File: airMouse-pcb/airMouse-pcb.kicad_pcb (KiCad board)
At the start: 2 copper layers, 54 parts, among them Q1 IRLML6346, SW1 TACT, SW10 TACT, SW11 TACT, SW12 TACT, SW13 TACT, SW14 TACT, SW15 TACT, SW16 TACT, SW17 TACT, SW18 TACT, SW19 TACT, SW2 TACT, SW20 TACT, SW21 TACT, SW22 TACT, SW23 TACT, SW24 TACT, SW25 TACT, SW26 TACT, SW27 TACT, SW28 TACT, SW29 TACT, SW3 TACT, SW30 TACT, SW31 TACT, SW32 TACT, SW33 TACT, SW34 TACT, SW35 TACT, SW36 TACT, SW37 TACT, SW38 TACT, SW39 TACT, SW4 TACT, SW40 TACT, SW41 TACT, SW42 TACT, SW43 TACT, SW44 TACT, SW45 TACT, SW46 TACT, SW47 TACT, SW48 TACT, SW49 TACT, SW5 TACT, SW6 TACT, SW7 TACT, SW8 TACT, SW9 TACT, U1 STM32G071RBTx, U2 AP1603

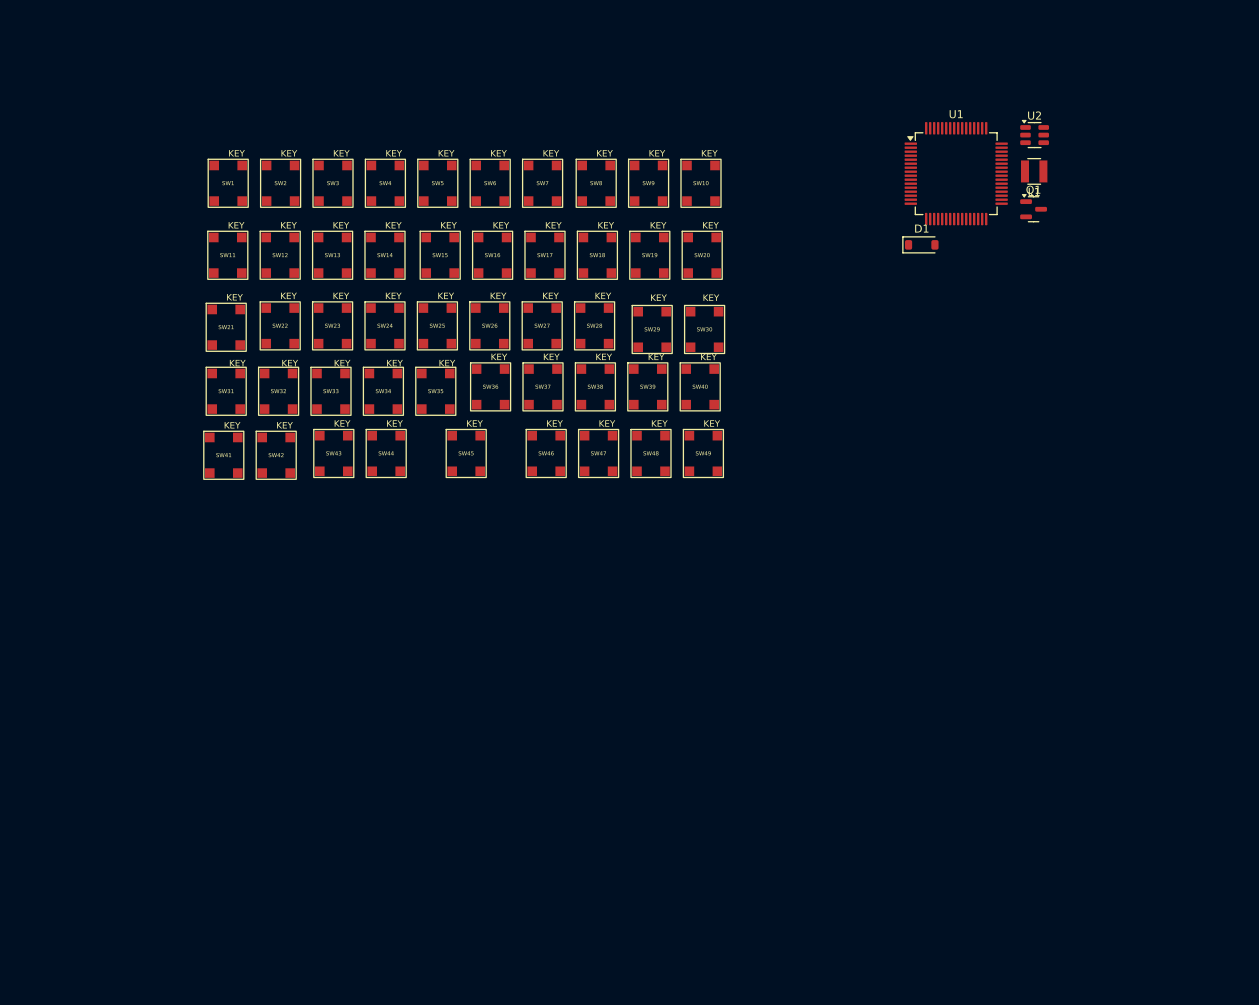
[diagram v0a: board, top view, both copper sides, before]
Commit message: add keyboard
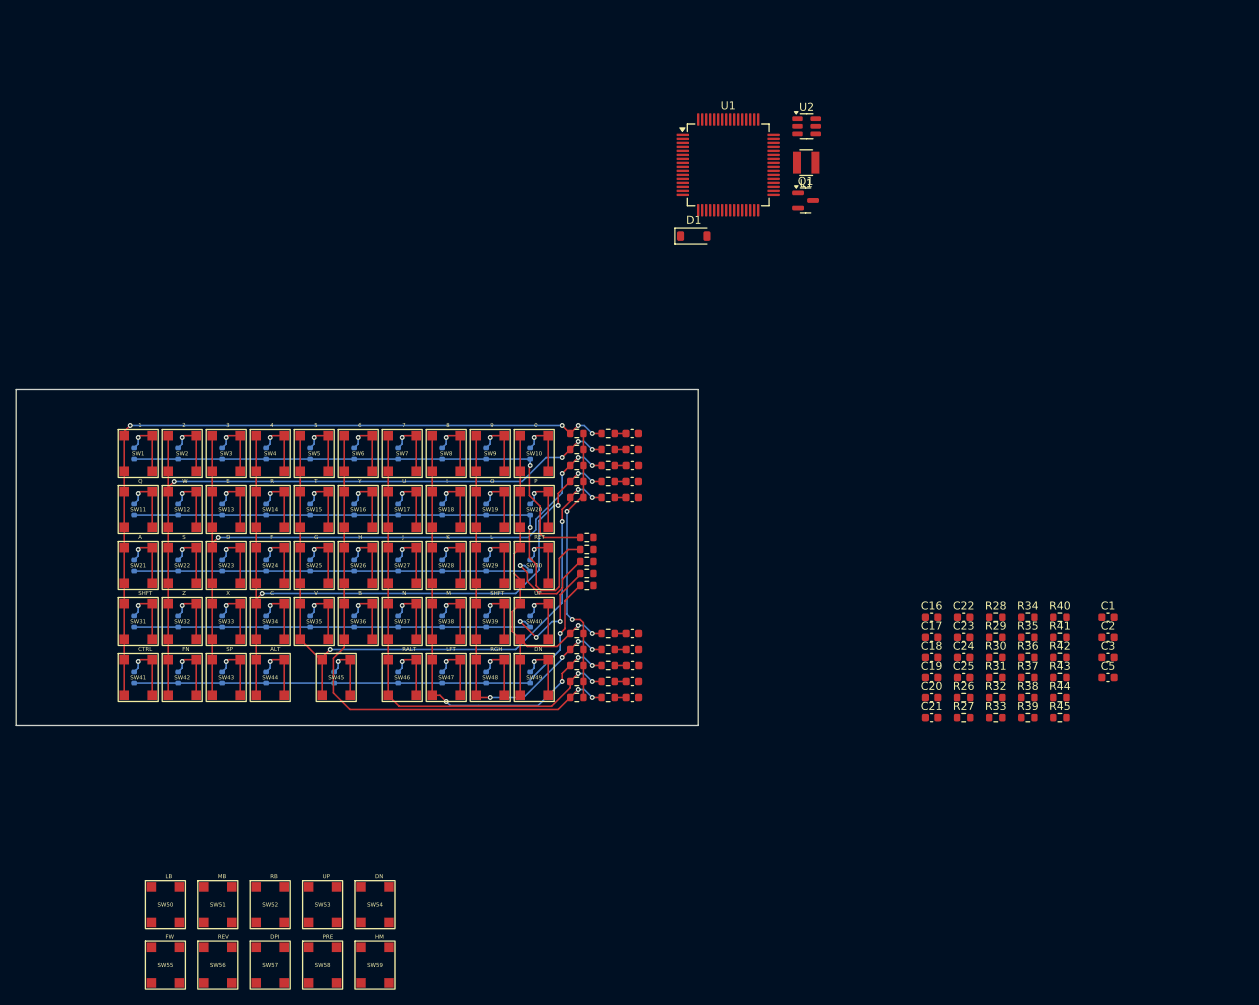
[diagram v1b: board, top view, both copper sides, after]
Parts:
- added C1: 105, Capacitor_SMD:C_0603_1608Metric, F.Cu at (210.2, 107.5)
- added C10: 100n, Capacitor_SMD:C_0603_1608Metric, F.Cu at (150.8, 115.5)
- added C11: 100n, Capacitor_SMD:C_0603_1608Metric, F.Cu at (150.8, 92.5)
- added C12: 100n, Capacitor_SMD:C_0603_1608Metric, F.Cu at (150.8, 90.5)
- added C13: 100n, Capacitor_SMD:C_0603_1608Metric, F.Cu at (150.8, 88.5)
- added C14: 100n, Capacitor_SMD:C_0603_1608Metric, F.Cu at (150.8, 86.5)
- added C15: 100n, Capacitor_SMD:C_0603_1608Metric, F.Cu at (150.8, 84.5)
- added C16: 100n, Capacitor_SMD:C_0603_1608Metric, F.Cu at (188.2, 107.5)
- added C17: 100n, Capacitor_SMD:C_0603_1608Metric, F.Cu at (188.2, 110.0)
- added C18: 100n, Capacitor_SMD:C_0603_1608Metric, F.Cu at (188.2, 112.5)
- added C19: 100n, Capacitor_SMD:C_0603_1608Metric, F.Cu at (188.2, 115.0)
- added C2: 100n, Capacitor_SMD:C_0603_1608Metric, F.Cu at (210.2, 110.0)
- added C20: 100n, Capacitor_SMD:C_0603_1608Metric, F.Cu at (188.2, 117.5)
- added C21: 100n, Capacitor_SMD:C_0603_1608Metric, F.Cu at (188.2, 120.0)
- added C22: 100n, Capacitor_SMD:C_0603_1608Metric, F.Cu at (192.2, 107.5)
- added C23: 100n, Capacitor_SMD:C_0603_1608Metric, F.Cu at (192.2, 110.0)
- added C24: 100n, Capacitor_SMD:C_0603_1608Metric, F.Cu at (192.2, 112.5)
- added C25: 100n, Capacitor_SMD:C_0603_1608Metric, F.Cu at (192.2, 115.0)
- added C3: 47u, Capacitor_SMD:C_0603_1608Metric, F.Cu at (210.2, 112.5)
- added C5: 100n, Capacitor_SMD:C_0603_1608Metric, F.Cu at (210.2, 115.0)
- added C6: 100n, Capacitor_SMD:C_0603_1608Metric, F.Cu at (150.8, 117.5)
- added C7: 100n, Capacitor_SMD:C_0603_1608Metric, F.Cu at (150.8, 109.5)
- added C8: 100n, Capacitor_SMD:C_0603_1608Metric, F.Cu at (150.8, 111.5)
- added C9: 100n, Capacitor_SMD:C_0603_1608Metric, F.Cu at (150.8, 113.5)
- added D10: BAS70X-TP, Diode_SMD:D_SOD-523, B.Cu at (132.5, 87.0)
- added D11: BAS70X-TP, Diode_SMD:D_SOD-523, B.Cu at (138.0, 87.0)
- added D14: BAS70X-TP, Diode_SMD:D_SOD-523, B.Cu at (88.5, 94.0)
- added D15: BAS70X-TP, Diode_SMD:D_SOD-523, B.Cu at (94.0, 94.0)
- added D16: BAS70X-TP, Diode_SMD:D_SOD-523, B.Cu at (99.5, 94.0)
- added D17: BAS70X-TP, Diode_SMD:D_SOD-523, B.Cu at (105.0, 94.0)
- added D18: BAS70X-TP, Diode_SMD:D_SOD-523, B.Cu at (88.5, 101.0)
- added D19: BAS70X-TP, Diode_SMD:D_SOD-523, B.Cu at (94.0, 101.0)
- added D2: BAS70X-TP, Diode_SMD:D_SOD-523, B.Cu at (88.5, 87.0)
- added D20: BAS70X-TP, Diode_SMD:D_SOD-523, B.Cu at (99.5, 101.0)
- added D21: BAS70X-TP, Diode_SMD:D_SOD-523, B.Cu at (105.0, 101.0)
- added D22: BAS70X-TP, Diode_SMD:D_SOD-523, B.Cu at (88.5, 108.0)
- added D23: BAS70X-TP, Diode_SMD:D_SOD-523, B.Cu at (94.0, 108.0)
- added D24: BAS70X-TP, Diode_SMD:D_SOD-523, B.Cu at (99.5, 108.0)
- added D25: BAS70X-TP, Diode_SMD:D_SOD-523, B.Cu at (105.0, 108.0)
- added D26: BAS70X-TP, Diode_SMD:D_SOD-523, B.Cu at (88.5, 115.0)
- added D27: BAS70X-TP, Diode_SMD:D_SOD-523, B.Cu at (94.0, 115.0)
- added D28: BAS70X-TP, Diode_SMD:D_SOD-523, B.Cu at (99.5, 115.0)
- added D29: BAS70X-TP, Diode_SMD:D_SOD-523, B.Cu at (105.0, 115.0)
- added D3: BAS70X-TP, Diode_SMD:D_SOD-523, B.Cu at (94.0, 87.0)
- added D30: BAS70X-TP, Diode_SMD:D_SOD-523, B.Cu at (110.5, 94.0)
- added D31: BAS70X-TP, Diode_SMD:D_SOD-523, B.Cu at (116.0, 94.0)
- added D32: BAS70X-TP, Diode_SMD:D_SOD-523, B.Cu at (121.5, 94.0)
- added D33: BAS70X-TP, Diode_SMD:D_SOD-523, B.Cu at (127.0, 94.0)
- added D34: BAS70X-TP, Diode_SMD:D_SOD-523, B.Cu at (110.5, 101.0)
- added D35: BAS70X-TP, Diode_SMD:D_SOD-523, B.Cu at (116.0, 101.0)
- added D36: BAS70X-TP, Diode_SMD:D_SOD-523, B.Cu at (121.5, 101.0)
- added D37: BAS70X-TP, Diode_SMD:D_SOD-523, B.Cu at (127.0, 101.0)
- added D38: BAS70X-TP, Diode_SMD:D_SOD-523, B.Cu at (110.5, 108.0)
- added D39: BAS70X-TP, Diode_SMD:D_SOD-523, B.Cu at (116.0, 108.0)
- added D4: BAS70X-TP, Diode_SMD:D_SOD-523, B.Cu at (99.5, 87.0)
- added D40: BAS70X-TP, Diode_SMD:D_SOD-523, B.Cu at (121.5, 108.0)
- added D41: BAS70X-TP, Diode_SMD:D_SOD-523, B.Cu at (127.0, 108.0)
- added D42: BAS70X-TP, Diode_SMD:D_SOD-523, B.Cu at (113.5, 115.0)
- added D44: BAS70X-TP, Diode_SMD:D_SOD-523, B.Cu at (121.5, 115.0)
- added D45: BAS70X-TP, Diode_SMD:D_SOD-523, B.Cu at (127.0, 115.0)
- added D46: BAS70X-TP, Diode_SMD:D_SOD-523, B.Cu at (132.5, 94.0)
- added D47: BAS70X-TP, Diode_SMD:D_SOD-523, B.Cu at (138.0, 94.0)
- added D5: BAS70X-TP, Diode_SMD:D_SOD-523, B.Cu at (105.0, 87.0)
- added D50: BAS70X-TP, Diode_SMD:D_SOD-523, B.Cu at (132.5, 101.0)
- added D51: BAS70X-TP, Diode_SMD:D_SOD-523, B.Cu at (138.0, 101.0)
- added D54: BAS70X-TP, Diode_SMD:D_SOD-523, B.Cu at (132.5, 108.0)
- added D55: BAS70X-TP, Diode_SMD:D_SOD-523, B.Cu at (138.0, 108.0)
- added D58: BAS70X-TP, Diode_SMD:D_SOD-523, B.Cu at (132.5, 115.0)
- added D59: BAS70X-TP, Diode_SMD:D_SOD-523, B.Cu at (138.0, 115.0)
- added D6: BAS70X-TP, Diode_SMD:D_SOD-523, B.Cu at (110.5, 87.0)
- added D7: BAS70X-TP, Diode_SMD:D_SOD-523, B.Cu at (116.0, 87.0)
- added D8: BAS70X-TP, Diode_SMD:D_SOD-523, B.Cu at (121.5, 87.0)
- added D9: BAS70X-TP, Diode_SMD:D_SOD-523, B.Cu at (127.0, 87.0)
- added R1: 100R, Resistor_SMD:R_0603_1608Metric, F.Cu at (145.1, 97.5)
- added R10: 10k, Resistor_SMD:R_0603_1608Metric, F.Cu at (143.8, 113.5)
- added R11: 10k, Resistor_SMD:R_0603_1608Metric, F.Cu at (143.8, 111.5)
- added R12: 10k, Resistor_SMD:R_0603_1608Metric, F.Cu at (143.8, 109.5)
- added R13: 100R, Resistor_SMD:R_0603_1608Metric, F.Cu at (145.1, 100.5)
- added R14: 100R, Resistor_SMD:R_0603_1608Metric, F.Cu at (145.1, 102.0)
- added R15: 100R, Resistor_SMD:R_0603_1608Metric, F.Cu at (145.1, 103.5)
- added R16: 10k, Resistor_SMD:R_0603_1608Metric, F.Cu at (147.8, 84.5)
- added R17: 10k, Resistor_SMD:R_0603_1608Metric, F.Cu at (147.8, 86.5)
- added R18: 10k, Resistor_SMD:R_0603_1608Metric, F.Cu at (147.8, 88.5)
- added R19: 10k, Resistor_SMD:R_0603_1608Metric, F.Cu at (147.8, 90.5)
- added R2: 100R, Resistor_SMD:R_0603_1608Metric, F.Cu at (145.1, 99.0)
- added R20: 10k, Resistor_SMD:R_0603_1608Metric, F.Cu at (147.8, 92.5)
- added R21: 10k, Resistor_SMD:R_0603_1608Metric, F.Cu at (147.8, 117.5)
- added R22: 10k, Resistor_SMD:R_0603_1608Metric, F.Cu at (147.8, 115.5)
- added R23: 10k, Resistor_SMD:R_0603_1608Metric, F.Cu at (147.8, 113.5)
- added R24: 10k, Resistor_SMD:R_0603_1608Metric, F.Cu at (147.8, 111.5)
- added R25: 10k, Resistor_SMD:R_0603_1608Metric, F.Cu at (147.8, 109.5)
- added R26: 10k, Resistor_SMD:R_0603_1608Metric, F.Cu at (192.2, 117.5)
- added R27: 10k, Resistor_SMD:R_0603_1608Metric, F.Cu at (192.2, 120.0)
- added R28: 10k, Resistor_SMD:R_0603_1608Metric, F.Cu at (196.2, 107.5)
- added R29: 10k, Resistor_SMD:R_0603_1608Metric, F.Cu at (196.2, 110.0)
- added R3: 10k, Resistor_SMD:R_0603_1608Metric, F.Cu at (143.8, 84.5)
- added R30: 10k, Resistor_SMD:R_0603_1608Metric, F.Cu at (196.2, 112.5)
- added R31: 10k, Resistor_SMD:R_0603_1608Metric, F.Cu at (196.2, 115.0)
- added R32: 10k, Resistor_SMD:R_0603_1608Metric, F.Cu at (196.2, 117.5)
- added R33: 10k, Resistor_SMD:R_0603_1608Metric, F.Cu at (196.2, 120.0)
- added R34: 10k, Resistor_SMD:R_0603_1608Metric, F.Cu at (200.2, 107.5)
- added R35: 10k, Resistor_SMD:R_0603_1608Metric, F.Cu at (200.2, 110.0)
- added R36: 10k, Resistor_SMD:R_0603_1608Metric, F.Cu at (200.2, 112.5)
- added R37: 10k, Resistor_SMD:R_0603_1608Metric, F.Cu at (200.2, 115.0)
- added R38: 10k, Resistor_SMD:R_0603_1608Metric, F.Cu at (200.2, 117.5)
- added R39: 10k, Resistor_SMD:R_0603_1608Metric, F.Cu at (200.2, 120.0)
- added R4: 10k, Resistor_SMD:R_0603_1608Metric, F.Cu at (143.8, 86.5)
- added R40: 10k, Resistor_SMD:R_0603_1608Metric, F.Cu at (204.2, 107.5)
- added R41: 10k, Resistor_SMD:R_0603_1608Metric, F.Cu at (204.2, 110.0)
- added R42: 10k, Resistor_SMD:R_0603_1608Metric, F.Cu at (204.2, 112.5)
- added R43: 10k, Resistor_SMD:R_0603_1608Metric, F.Cu at (204.2, 115.0)
- added R44: 10k, Resistor_SMD:R_0603_1608Metric, F.Cu at (204.2, 117.5)
- added R45: 10k, Resistor_SMD:R_0603_1608Metric, F.Cu at (204.2, 120.0)
- added R5: 10k, Resistor_SMD:R_0603_1608Metric, F.Cu at (143.8, 88.5)
- added R6: 10k, Resistor_SMD:R_0603_1608Metric, F.Cu at (143.8, 90.5)
- added R7: 10k, Resistor_SMD:R_0603_1608Metric, F.Cu at (143.8, 92.5)
- added R8: 10k, Resistor_SMD:R_0603_1608Metric, F.Cu at (143.8, 117.5)
- added R9: 10k, Resistor_SMD:R_0603_1608Metric, F.Cu at (143.8, 115.5)
- added SW50: KEY, airMouseLib:TL3315NF100Q, F.Cu at (92.4, 143.4)
- added SW51: KEY, airMouseLib:TL3315NF100Q, F.Cu at (99.0, 143.4)
- added SW52: KEY, airMouseLib:TL3315NF100Q, F.Cu at (105.5, 143.4)
- added SW53: KEY, airMouseLib:TL3315NF100Q, F.Cu at (112.0, 143.4)
- added SW54: KEY, airMouseLib:TL3315NF100Q, F.Cu at (118.6, 143.4)
- added SW55: KEY, airMouseLib:TL3315NF100Q, F.Cu at (92.4, 150.9)
- added SW56: KEY, airMouseLib:TL3315NF100Q, F.Cu at (99.0, 150.9)
- added SW57: KEY, airMouseLib:TL3315NF100Q, F.Cu at (105.5, 150.9)
- added SW58: KEY, airMouseLib:TL3315NF100Q, F.Cu at (112.0, 150.9)
- added SW59: KEY, airMouseLib:TL3315NF100Q, F.Cu at (118.6, 150.9)
- SW1, SW10, SW11, SW12, SW13, SW14, SW15, SW16, SW17, SW18, SW19, SW2, SW20, SW21, SW22, SW23, SW24, SW25, SW26, SW27, SW28, SW29, SW3, SW30, SW31, SW32, SW33, SW34, SW35, SW36, SW37, SW38, SW39, SW4, SW40, SW41, SW42, SW43, SW44, SW45, SW46, SW47, SW48, SW49, SW5, SW6, SW7, SW8, SW9: value TACT -> KEY
- moved SW10 39.7 mm to (138.5, 87.0)
- moved SW9 39.2 mm to (133.0, 87.0)
- moved SW8 38.6 mm to (127.5, 87.0)
- moved SW20 38.1 mm to (138.5, 94.0)
- moved SW7 38.1 mm to (122.0, 87.0)
- moved SW6 37.6 mm to (116.5, 87.0)
- moved SW19 37.5 mm to (133.0, 94.0)
- moved SW5 37.1 mm to (111.0, 87.0)
- moved SW18 37.0 mm to (127.5, 94.0)
- moved SW4 36.7 mm to (105.5, 87.0)
- moved SW17 36.4 mm to (122.0, 94.0)
- moved SW30 36.4 mm to (138.5, 101.0)
- moved SW3 36.3 mm to (100.0, 87.0)
- moved SW2 35.9 mm to (94.5, 87.0)
- moved SW16 35.9 mm to (116.5, 94.0)
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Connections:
- SW1 pad 2: Net-(SW1-B) -> Net-(D2-A)
- SW10 pad 2: Net-(SW1-B) -> Net-(D11-A)
- SW11 pad 2: Net-(SW11-B) -> Net-(D14-A)
- SW12 pad 2: Net-(SW11-B) -> Net-(D15-A)
- SW13 pad 2: Net-(SW11-B) -> Net-(D16-A)
- SW14 pad 2: Net-(SW11-B) -> Net-(D17-A)
- SW15 pad 2: Net-(SW11-B) -> Net-(D30-A)
- SW16 pad 2: Net-(SW11-B) -> Net-(D31-A)
- SW17 pad 2: Net-(SW11-B) -> Net-(D32-A)
- SW18 pad 2: Net-(SW11-B) -> Net-(D33-A)
- SW19 pad 2: Net-(SW11-B) -> Net-(D46-A)
- SW2 pad 2: Net-(SW1-B) -> Net-(D3-A)
- SW20 pad 2: Net-(SW11-B) -> Net-(D47-A)
- SW21 pad 2: Net-(SW21-B) -> Net-(D18-A)
- SW22 pad 2: Net-(SW21-B) -> Net-(D19-A)
- SW23 pad 2: Net-(SW21-B) -> Net-(D20-A)
- SW24 pad 2: Net-(SW21-B) -> Net-(D21-A)
- SW25 pad 2: Net-(SW21-B) -> Net-(D34-A)
- SW26 pad 2: Net-(SW21-B) -> Net-(D35-A)
- SW27 pad 2: Net-(SW21-B) -> Net-(D36-A)
- SW28 pad 2: Net-(SW21-B) -> Net-(D37-A)
- SW29 pad 2: Net-(SW21-B) -> Net-(D50-A)
- SW3 pad 2: Net-(SW1-B) -> Net-(D4-A)
- SW30 pad 2: Net-(SW21-B) -> Net-(D51-A)
- SW31 pad 2: Net-(SW31-B) -> Net-(D22-A)
- SW32 pad 2: Net-(SW31-B) -> Net-(D23-A)
- SW33 pad 2: Net-(SW31-B) -> Net-(D24-A)
- SW34 pad 2: Net-(SW31-B) -> Net-(D25-A)
- SW35 pad 2: Net-(SW31-B) -> Net-(D38-A)
- SW36 pad 2: Net-(SW31-B) -> Net-(D39-A)
- SW37 pad 2: Net-(SW31-B) -> Net-(D40-A)
- SW38 pad 2: Net-(SW31-B) -> Net-(D41-A)
- SW39 pad 2: Net-(SW31-B) -> Net-(D54-A)
- SW4 pad 2: Net-(SW1-B) -> Net-(D5-A)
- SW40 pad 2: Net-(SW31-B) -> Net-(D55-A)
- SW41 pad 2: Net-(SW12-A) -> Net-(D26-A)
- SW42 pad 2: Net-(SW42-B) -> Net-(D27-A)
- SW43 pad 2: Net-(SW42-B) -> Net-(D28-A)
- SW44 pad 2: Net-(SW42-B) -> Net-(D29-A)
- SW45 pad 1: Net-(SW16-A) -> Net-(SW15-A)
- SW45 pad 2: Net-(SW42-B) -> Net-(D42-A)
- SW46 pad 2: Net-(SW42-B) -> Net-(D44-A)
- SW47 pad 2: Net-(SW42-B) -> Net-(D45-A)
- SW48 pad 2: Net-(SW42-B) -> Net-(D58-A)
- SW49 pad 2: Net-(SW42-B) -> Net-(D59-A)
- SW5 pad 2: Net-(SW1-B) -> Net-(D6-A)
- SW6 pad 2: Net-(SW1-B) -> Net-(D7-A)
- SW7 pad 2: Net-(SW1-B) -> Net-(D8-A)
- SW8 pad 2: Net-(SW1-B) -> Net-(D9-A)
- SW9 pad 2: Net-(SW1-B) -> Net-(D10-A)
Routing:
- net Net-(SW1-A): track 0.00 -> 94.2 mm, vias 0 -> 4
- net Net-(SW12-A): track 0.00 -> 89.9 mm, vias 0 -> 4
- net Net-(SW13-A): track 0.00 -> 88.7 mm, vias 0 -> 4
- net Net-(SW14-A): track 0.00 -> 87.6 mm, vias 0 -> 4
- net Net-(SW15-A): track 0.00 -> 85.2 mm, vias 0 -> 4
- net Net-(D14-K): track 0.00 -> 68.7 mm, vias 0 -> 1
- net Net-(SW16-A): track 0.00 -> 68.5 mm, vias 0 -> 2
- net Net-(D22-K): track 0.00 -> 64.7 mm, vias 0 -> 3
- net Net-(D10-K): track 0.00 -> 64.6 mm, vias 0 -> 1
- net Net-(D26-K): track 0.00 -> 64.3 mm, vias 0 -> 1
- net Net-(D18-K): track 0.00 -> 63.0 mm, vias 0 -> 1
- net Net-(SW17-A): track 0.00 -> 62.3 mm, vias 0 -> 2
- net Net-(SW18-A): track 0.00 -> 57.6 mm, vias 0 -> 4
- net Net-(SW19-A): track 0.00 -> 51.7 mm, vias 0 -> 4
- net Net-(SW10-A): track 0.00 -> 45.9 mm, vias 0 -> 2
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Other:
- board outline added: 85.2 x 42 mm

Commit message: schematic
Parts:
- added BT1: BC-0401, airMouseLib:BC-0401, F.Cu at (106.1, 42.1)
- added C26: 100n, Capacitor_SMD:C_0603_1608Metric, F.Cu at (114.6, 49.4)
- added C27: 4u7, Capacitor_SMD:C_0805_2012Metric, F.Cu at (98.6, 65.5)
- added C28: 1u, Capacitor_SMD:C_0603_1608Metric, F.Cu at (114.6, 51.9)
- added C29: 100n, Capacitor_SMD:C_0603_1608Metric, F.Cu at (114.6, 54.4)
- added C30: 1u, Capacitor_SMD:C_0603_1608Metric, F.Cu at (114.6, 56.9)
- added C31: 100n, Capacitor_SMD:C_0603_1608Metric, F.Cu at (114.6, 59.4)
- added C32: 10u, Capacitor_SMD:C_0805_2012Metric, F.Cu at (98.6, 68.5)
- added C33: 100n, Capacitor_SMD:C_0603_1608Metric, F.Cu at (118.6, 49.4)
- added C34: 100n, Capacitor_SMD:C_0603_1608Metric, F.Cu at (118.6, 51.9)
- added C4: 47u, Capacitor_SMD:CP_Elec_6.3x5.8, F.Cu at (87.1, 68.0)
- added D12: STBY, LED_SMD:LED_0603_1608Metric, F.Cu at (94.3, 65.3)
- added D13: BT, LED_SMD:LED_0603_1608Metric, F.Cu at (94.3, 67.9)
- added D43: LOW_BAT, LED_SMD:LED_0603_1608Metric, F.Cu at (94.3, 70.5)
- added FB1: 600R @ 100M, Capacitor_SMD:C_0603_1608Metric, F.Cu at (118.6, 54.4)
- added J4: AT, Connector_JST:JST_ZH_S3B-ZR-SM4A-TF_1x03-1MP_P1.50mm_Horizontal, F.Cu at (107.6, 52.1)
- added J5: RADIO_PRG, Connector_JST:JST_ZH_S3B-ZR-SM4A-TF_1x03-1MP_P1.50mm_Horizontal, F.Cu at (107.6, 61.2)
- added J6: MCU_PRG, Connector_JST:JST_ZH_S5B-ZR-SM4A-TF_1x05-1MP_P1.50mm_Horizontal, F.Cu at (123.8, 64.7)
- added LD1: 70115420, Connector_PinHeader_2.54mm:PinHeader_1x02_P2.54mm_Vertical, F.Cu at (115.0, 63.0)
- added R46: 2k2, Resistor_SMD:R_0603_1608Metric, F.Cu at (118.6, 56.9)
- added R47: 2k2, Resistor_SMD:R_0603_1608Metric, F.Cu at (118.6, 59.4)
- added R48: 2k2, Resistor_SMD:R_0603_1608Metric, F.Cu at (122.7, 49.4)
- added R49: 10k, Resistor_SMD:R_0603_1608Metric, F.Cu at (122.7, 51.9)
- added R50: 10k, Resistor_SMD:R_0603_1608Metric, F.Cu at (122.7, 54.4)
- added R51: 4k7, Resistor_SMD:R_0603_1608Metric, F.Cu at (122.7, 56.9)
- added R52: 4k7, Resistor_SMD:R_0603_1608Metric, F.Cu at (122.7, 59.4)
- added R53: 10k, Resistor_SMD:R_0603_1608Metric, F.Cu at (126.7, 49.4)
- added R54: 10k, Resistor_SMD:R_0603_1608Metric, F.Cu at (126.7, 51.9)
- added R55: 10k, Resistor_SMD:R_0603_1608Metric, F.Cu at (126.7, 54.4)
- added R56: 10k, Resistor_SMD:R_0603_1608Metric, F.Cu at (126.7, 56.9)
- added R57: 2k2, Resistor_SMD:R_0603_1608Metric, F.Cu at (126.7, 59.4)
- added R58: 10k, Resistor_SMD:R_0603_1608Metric, F.Cu at (222.0, 72.2)
- added R59: 10k, Resistor_SMD:R_0603_1608Metric, F.Cu at (222.0, 74.7)
- added R60: 0R, Resistor_SMD:R_0603_1608Metric, F.Cu at (222.0, 77.2)
- added R61: 0R, Resistor_SMD:R_0603_1608Metric, F.Cu at (222.0, 79.7)
- added SW60: KEY, airMouseLib:TL3315NF100Q, F.Cu at (105.8, 70.0)
- added TP1: DBG_TX, TestPoint:TestPoint_Pad_D1.0mm, F.Cu at (225.5, 72.5)
- added TP2: DBG_RX, TestPoint:TestPoint_Pad_D1.0mm, F.Cu at (225.5, 75.5)
- added U3: ESP32-C3-WROOM-02U, RF_Module:ESP32-C3-WROOM-02U, F.Cu at (92.3, 56.3)
- added U4: LSM6DS3, Package_LGA:LGA-14_3x2.5mm_P0.5mm_LayoutBorder3x4y, F.Cu at (98.7, 72.1)
- C3: footprint Capacitor_SMD:C_0603_1608Metric -> Capacitor_SMD:CP_Elec_6.3x5.8
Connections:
- net /INPUT renamed /BAT+
- net Net-(BT1--) renamed /BAT-
- C10 pad 1: /Keyboard/KEY_COL7 -> /COL7
- C11 pad 1: /Keyboard/KEY_COL5 -> /COL5
- C12 pad 1: /Keyboard/KEY_COL4 -> /COL4
- C13 pad 1: /Keyboard/KEY_COL3 -> /COL3
- C14 pad 1: /Keyboard/KEY_COL2 -> /COL2
- C15 pad 1: /Keyboard/KEY_COL1 -> /COL1
- C6 pad 1: /Keyboard/KEY_COL6 -> /COL6
- C7 pad 1: /Keyboard/KEY_COL10 -> /COL10
- C8 pad 1: /Keyboard/KEY_COL9 -> /COL9
- C9 pad 1: /Keyboard/KEY_COL8 -> /COL8
- R16 pad 2: /Keyboard/KEY_COL1 -> /COL1
- R17 pad 2: /Keyboard/KEY_COL2 -> /COL2
- R18 pad 2: /Keyboard/KEY_COL3 -> /COL3
- R19 pad 2: /Keyboard/KEY_COL4 -> /COL4
- R20 pad 2: /Keyboard/KEY_COL5 -> /COL5
- R21 pad 2: /Keyboard/KEY_COL6 -> /COL6
- R22 pad 2: /Keyboard/KEY_COL7 -> /COL7
- R23 pad 2: /Keyboard/KEY_COL8 -> /COL8
- R24 pad 2: /Keyboard/KEY_COL9 -> /COL9
- R25 pad 2: /Keyboard/KEY_COL10 -> /COL10
- U1 pad 1: unconnected-(U1-PC11-Pad1) -> /mouse/MOUSE_FWD
- U1 pad 12: unconnected-(U1-PF2-Pad12) -> /RST
- U1 pad 14: /Keyboard/KEY_COL1 -> unconnected-(U1-PC1-Pad14)
- U1 pad 15: /Keyboard/KEY_COL2 -> unconnected-(U1-PC2-Pad15)
- U1 pad 16: /Keyboard/KEY_COL3 -> unconnected-(U1-PC3-Pad16)
- U1 pad 17: unconnected-(U1-PA0-Pad17) -> /GYRO_INT
- U1 pad 18: unconnected-(U1-PA1-Pad18) -> Net-(D13-A)
- U1 pad 19: unconnected-(U1-PA2-Pad19) -> /DBG_TX
- U1 pad 2: unconnected-(U1-PC12-Pad2) -> /mouse/MOUSE_BACK
- U1 pad 20: unconnected-(U1-PA3-Pad20) -> /DBR_RX
- U1 pad 21: unconnected-(U1-PA4-Pad21) -> Net-(D43-A)
- U1 pad 22: unconnected-(U1-PA5-Pad22) -> Net-(D12-A)
- U1 pad 25: /Keyboard/KEY_COL4 -> /AT_MCU_TX
- U1 pad 26: /Keyboard/KEY_COL5 -> /AT_MCU_RX
- U1 pad 28: unconnected-(U1-PB1-Pad28) -> /COL1
- U1 pad 29: unconnected-(U1-PB2-Pad29) -> /COL2
- U1 pad 3: unconnected-(U1-PC13-Pad3) -> /mouse/MOUSE_DPI
- U1 pad 30: unconnected-(U1-PB10-Pad30) -> /COL10
- U1 pad 34: unconnected-(U1-PB14-Pad34) -> /ESP_BOOT
- U1 pad 35: unconnected-(U1-PB15-Pad35) -> /ESP_RST
- U1 pad 37: unconnected-(U1-PA9/UCPD1_DBCC1-Pad37) -> /SCL
- U1 pad 38: /Keyboard/KEY_COL6 -> /mouse/MOUSE_LB
- U1 pad 39: /Keyboard/KEY_COL7 -> /mouse/MOUSE_MB
- U1 pad 4: unconnected-(U1-PC14-Pad4) -> /mouse/MOUSE_PRC
- U1 pad 42: unconnected-(U1-PA10/UCPD1_DBCC2-Pad42) -> /SDA
- U1 pad 45: unconnected-(U1-PA13-Pad45) -> /SWDIO
- U1 pad 46: unconnected-(U1-PA14-Pad46) -> /SWDCLK
- U1 pad 48: /Keyboard/KEY_COL8 -> /mouse/MOUSE_RB
- U1 pad 49: /Keyboard/KEY_COL9 -> /mouse/MOUSE_UP
- U1 pad 5: unconnected-(U1-PC15-Pad5) -> /mouse/MOUSE_HOME
- U1 pad 57: unconnected-(U1-PB3-Pad57) -> /COL3
- U1 pad 58: unconnected-(U1-PB4-Pad58) -> /COL4
- U1 pad 59: unconnected-(U1-PB5-Pad59) -> /COL5
- U1 pad 6: unconnected-(U1-VBAT-Pad6) -> +3V3
- U1 pad 60: unconnected-(U1-PB6-Pad60) -> /COL6
- U1 pad 61: unconnected-(U1-PB7-Pad61) -> /COL7
- U1 pad 62: unconnected-(U1-PB8-Pad62) -> /COL8
- U1 pad 63: unconnected-(U1-PB9-Pad63) -> /COL9
- U1 pad 64: /Keyboard/KEY_COL10 -> /mouse/MOUSE_DN
- U1 pad 7: unconnected-(U1-VREF+-Pad7) -> Net-(U1-VREF+)
- U1 pad 8: unconnected-(U1-VDD-Pad8) -> +3V3
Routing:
- net /Keyboard/KEY_COL8: track 1.45 -> 0.00 mm
- net /COL8: track 0.00 -> 1.45 mm
- net /Keyboard/KEY_COL9: track 1.43 -> 0.00 mm
- net /Keyboard/KEY_COL7: track 1.43 -> 0.00 mm
- net /Keyboard/KEY_COL6: track 1.43 -> 0.00 mm
- net /Keyboard/KEY_COL3: track 1.43 -> 0.00 mm
- net /Keyboard/KEY_COL10: track 1.43 -> 0.00 mm
- net /COL9: track 0.00 -> 1.43 mm
- net /COL7: track 0.00 -> 1.43 mm
- net /COL6: track 0.00 -> 1.43 mm
- net /COL3: track 0.00 -> 1.43 mm
- net /COL10: track 0.00 -> 1.43 mm
- net /Keyboard/KEY_COL5: track 1.40 -> 0.00 mm
- net /Keyboard/KEY_COL4: track 1.40 -> 0.00 mm
- net /Keyboard/KEY_COL2: track 1.40 -> 0.00 mm
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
